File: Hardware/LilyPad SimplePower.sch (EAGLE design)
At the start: 20 parts, among them U1 MCP73831

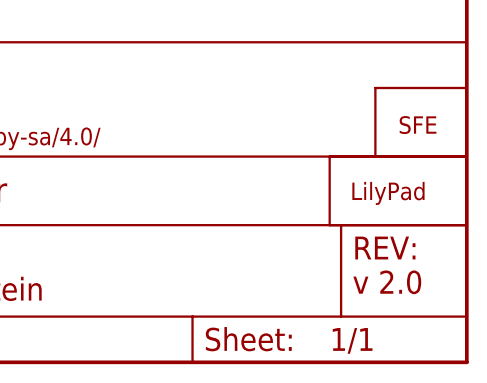
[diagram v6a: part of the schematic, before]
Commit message: Updating bRestrict to give Lilypad petal pattern
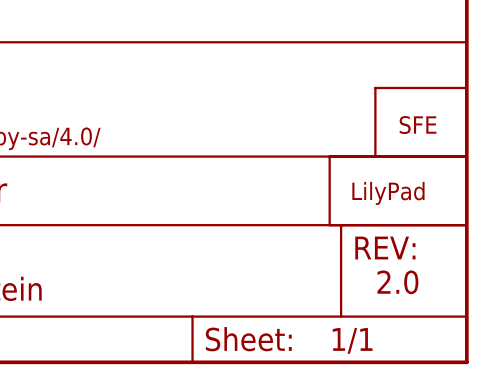
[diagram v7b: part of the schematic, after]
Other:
- note added: "2.0"
- note removed: "v 2.0"
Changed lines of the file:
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@@
 <plain>
 <text x="171.704" y="11.684" size="2.54" layer="94">Nathan Seidle</text>
-<text x="236.22" y="7.62" size="2.54" layer="94">v 2.0</text>
+<text x="238.76" y="7.62" size="2.54" layer="94">2.0</text>
 <text x="174.752" y="6.858" size="2.54" layer="94">Toni Klopfenstein</text>
 <wire x1="0" y1="50.8" x2="53.34" y2="50.8" width="0.2032" layer="94" style="shortdash"/>

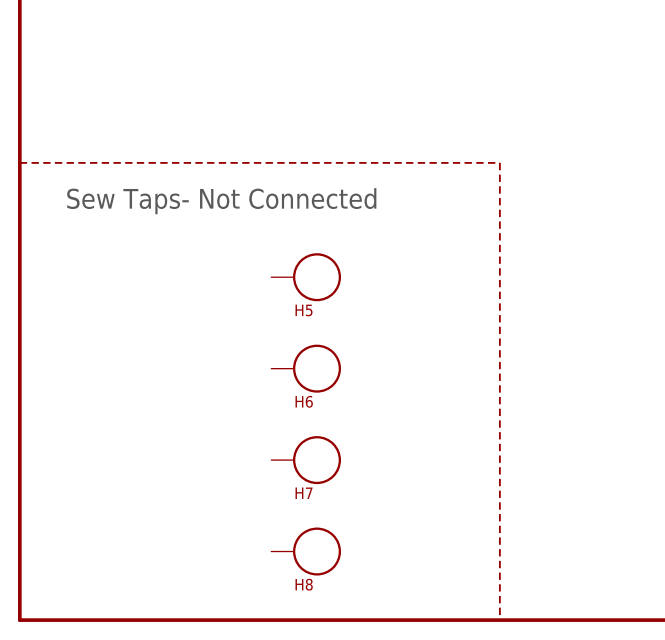
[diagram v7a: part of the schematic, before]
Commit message: Updating board with more classic LilyPad design
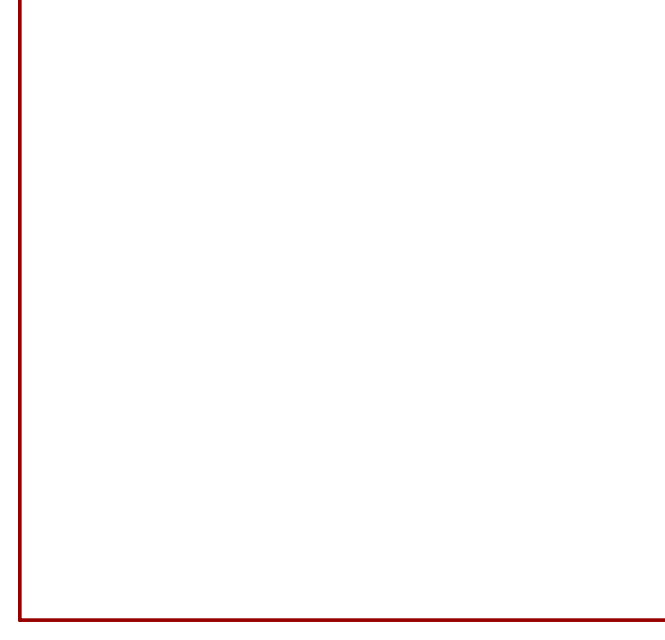
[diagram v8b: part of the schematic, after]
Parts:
- removed H5, H6, H7, H8: SEW_HOLE, LilyPad-Wearables:SEW_HOLE
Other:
- note removed: "Sew Taps- Not Connected"
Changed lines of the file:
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@@
 <?xml version="1.0" encoding="utf-8"?>
 <!DOCTYPE eagle SYSTEM "eagle.dtd">
-<eagle version="6.5.0">
+<eagle version="6.6.0">
 <drawing>
 <settings>
@@
 <part name="U$3" library="LilyPad-Wearables" deviceset="SEWTAP" device="9" value="SEWTAP9"/>
 <part name="U$4" library="LilyPad-Wearables" deviceset="SEWTAP" device="9" value="SEWTAP9"/>
-<part name="U$1" library="LilyPad-Wearables" deviceset="LOGO-LP" device="LP" value="LOGO-LPLP"/>
 <part name="U$5" library="SparkFun-Aesthetics" deviceset="OSHW-LOGO" device="S"/>
 <part name="JP3" library="SparkFun-Aesthetics" deviceset="LOGO-SFE" device="SK"/>
@@
 <part name="GND5" library="SparkFun-Aesthetics" deviceset="GND" device=""/>
 <part name="U$6" library="SparkFun-Aesthetics" deviceset="REVISION" device=""/>
-<part name="H5" library="LilyPad-Wearables" deviceset="SEW_HOLE" device=""/>
-<part name="H6" library="LilyPad-Wearables" deviceset="SEW_HOLE" device=""/>
-<part name="H7" library="LilyPad-Wearables" deviceset="SEW_HOLE" device=""/>
-<part name="H8" library="LilyPad-Wearables" deviceset="SEW_HOLE" device=""/>
+<part name="U$1" library="LilyPad-Wearables" deviceset="LOGO-LP" device="LP"/>
 </parts>
 <sheets>
@@
 <text x="238.76" y="7.62" size="2.54" layer="94">2.0</text>
 <text x="174.752" y="6.858" size="2.54" layer="94">Toni Klopfenstein</text>
-<wire x1="0" y1="50.8" x2="53.34" y2="50.8" width="0.2032" layer="94" style="shortdash"/>
-<wire x1="53.34" y1="50.8" x2="53.34" y2="0" width="0.2032" layer="94" style="shortdash"/>
-<text x="5.08" y="45.72" size="2.1844" layer="97">Sew Taps- Not Connected</text>
 <text x="116.84" y="132.08" size="1.9304" layer="97">Charging Rate = 500 mA</text>
 </plain>
@@
 <instance part="U$3" gate="G$1" x="218.44" y="86.36"/>
 <instance part="U$4" gate="G$1" x="210.82" y="111.76"/>
-<instance part="U$1" gate="G$1" x="236.22" y="17.78"/>
 <instance part="U$5" gate="G$1" x="134.62" y="10.16"/>
 <instance part="JP3" gate="G$1" x="241.3" y="25.4"/>
@@
 <instance part="GND5" gate="1" x="157.48" y="96.52"/>
 <instance part="U$6" gate="G$1" x="148.082" y="6.858"/>
-<instance part="H5" gate="G$1" x="33.02" y="38.1"/>
-<instance part="H6" gate="G$1" x="33.02" y="27.94"/>
-<instance part="H7" gate="G$1" x="33.02" y="17.78"/>
-<instance part="H8" gate="G$1" x="33.02" y="7.62"/>
+<instance part="U$1" gate="G$1" x="236.22" y="17.78"/>
 </instances>
 <busses>
